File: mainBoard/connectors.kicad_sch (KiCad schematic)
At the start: 69 parts, among them J10 Conn_01x02, J11 Conn_02x05_Odd_Even, J12 Conn_01x02, J14 Conn_01x06, J15 Conn_01x03, J17 Conn_01x05, J18 Conn_01x04, J19 Conn_01x14, J8 Conn_01x02, J9 Conn_01x02, Q3 IRLML6244TRPBF, Q4 IRLML6244TRPBF, Q5 IRLML6244TRPBF, Q8 PMOS, U17 SFH617A-2, U18 USBLC6-4SC6, U20 LM386, U21 USBLC6-4SC6, U23 USBLC6-4SC6, U24 USBLC6-2SC6, U26 100, U27 100, U28 100, U29 100, U30 74LVC1T45W6-7, U32 74LVC1T45W6-7

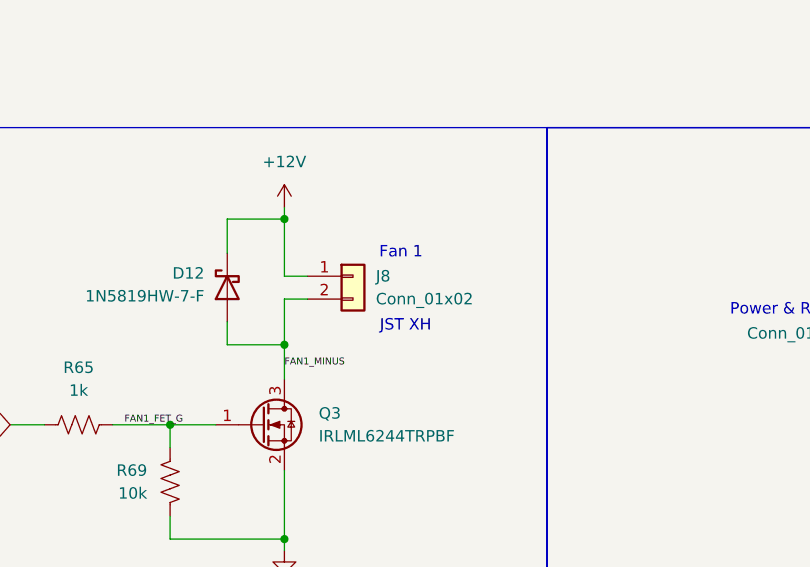
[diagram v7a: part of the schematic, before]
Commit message: flip j8 for fan 1
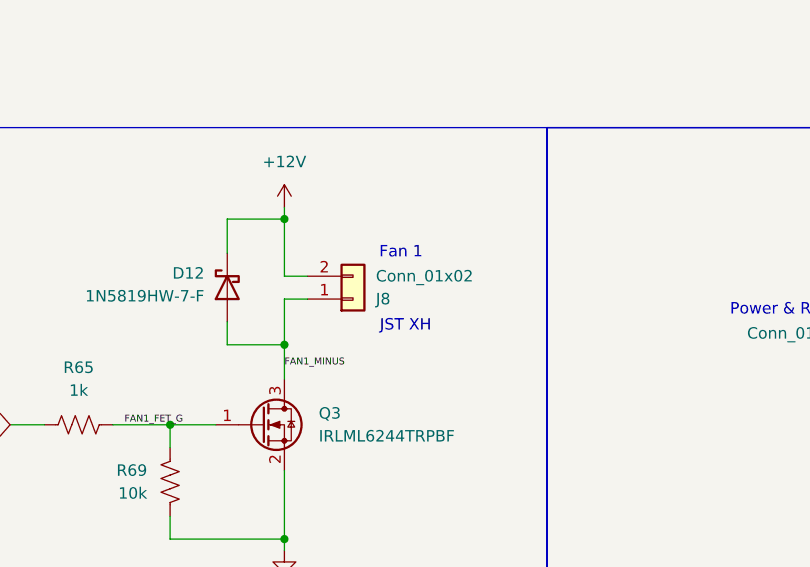
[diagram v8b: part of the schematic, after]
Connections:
- net +12V: now also J8.2 (Pin_2); no longer J8.1 (Pin_1)
- net FAN1_MINUS: now also J8.1 (Pin_1); no longer J8.2 (Pin_2)
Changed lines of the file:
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@@
 	(symbol
 		(lib_id "Connector_Generic:Conn_01x02")
-		(at 85.09 55.88 0)
+		(at 85.09 58.42 0)
+		(mirror x)
 		(unit 1)
 		(body_style 1)
@@
 		(in_pos_files yes)
 		(dnp no)
-		(fields_autoplaced yes)
 		(property "Reference" "J8"
-			(at 87.63 55.8799 0)
+			(at 87.63 58.4201 0)
 			(show_name no)
 			(do_not_autoplace no)
@@
 		)
 		(property "Value" "Conn_01x02"
-			(at 87.63 58.4199 0)
+			(at 87.63 55.8801 0)
 			(show_name no)
 			(do_not_autoplace no)
@@
 		)
 		(property "Footprint" "Connector_JST:JST_XH_B2B-XH-A_1x02_P2.50mm_Vertical"
-			(at 85.09 55.88 0)
+			(at 85.09 58.42 0)
 			(hide yes)
 			(show_name no)
@@
 		)
 		(property "Datasheet" ""
-			(at 85.09 55.88 0)
+			(at 85.09 58.42 0)
 			(hide yes)
 			(show_name no)
@@
 		)
 		(property "Description" "Generic connector, single row, 01x02, script generated (kicad-library-utils/schlib/autogen/connector/)"
-			(at 85.09 55.88 0)
+			(at 85.09 58.42 0)
 			(hide yes)
 			(show_name no)
